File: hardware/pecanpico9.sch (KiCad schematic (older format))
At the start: 119 parts, among them IC1 SPV1040T, IC2 TPS62260DRVR, IC3 ADP322ACPZ-115-R7, IC4 Si4063-B1B-FM, IC5 STM32F413xG, IC6 EVA-7M, IC7 PAC1720-1-AIA-TR, IC8 LDLN015PU33R, IC9 BME280, P1 CONN_01X25, P2 CONN_01X10, P3 ZX62-B-5PA(33), P4 IPX 2mm, P5 CONN_01X02, P6 IPX 2mm, Q1 FDN306P, X1 KT2016K26000BCW18ZAS

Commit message: Wiggled parts around
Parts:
- removed W12, W13, W14, W15, W16, W17, W19, W21, W22, W23, W26, W27: Testpad, stm32f7:Testpad, symbol TEST_1P
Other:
- note added: "Camera connector and Atmosphere sensor"
- note removed: "Camera edge connector and daugther board (camera + additional BME280)"
- note removed: "Clock CTRL may be used to modulate\nthe Si4063. It may also influence the\nclock of the STM32 but only slightly."
- moved on the sheet: C30, C31, C32, C33, C34, C35, C37, C38, C39, C40, C43, C44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

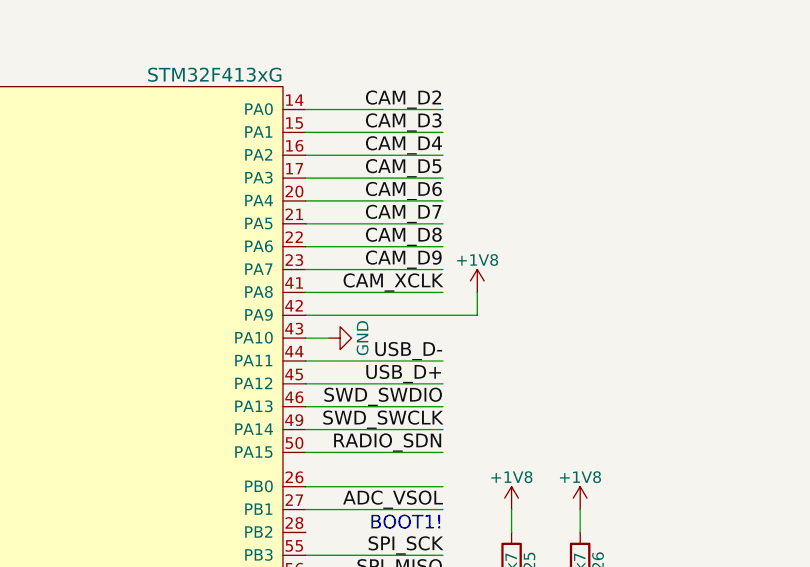
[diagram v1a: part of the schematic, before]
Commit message: Connected VUSB correctly to PA9
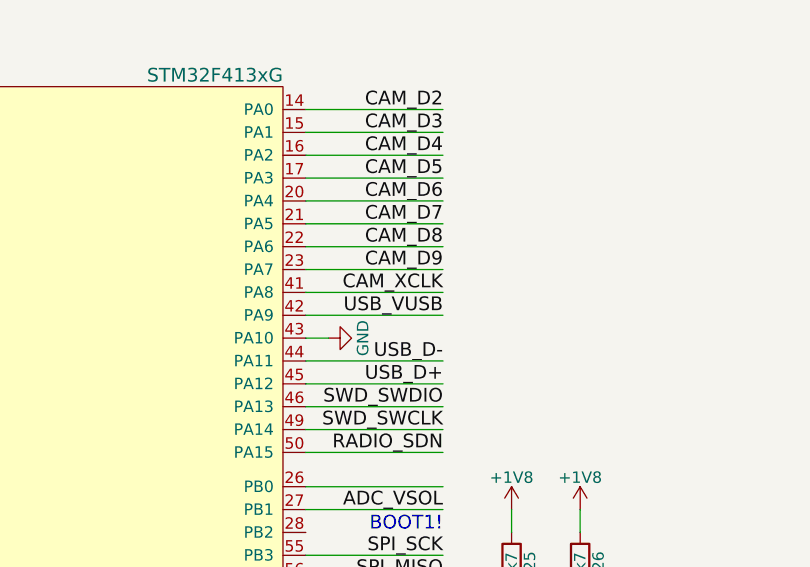
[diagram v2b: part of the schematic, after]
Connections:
- net +1V8: no longer IC5.42 (PA9)
- net USB_VUSB: now also IC5.42 (PA9)
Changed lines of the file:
@@
 BOOT1!
-$Comp
-L +1V8 #PWR097
-U 1 1 58F7653D
-P 19350 4050
-F 0 "#PWR097" H 19350 3900 50  0001 C CNN
-F 1 "+1V8" H 19350 4190 50  0000 C CNN
-F 2 "" H 19350 4050 50  0000 C CNN
-F 3 "" H 19350 4050 50  0000 C CNN
-	1    19350 4050
-	1    0    0    -1
-$EndComp
 $Comp
 L C C35
@@
 $EndComp
 $Comp
-L GND #PWR098
+L GND #PWR097
 U 1 1 58F46541
 P 15000 3650
-F 0 "#PWR098" H 15000 3400 50  0001 C CNN
+F 0 "#PWR097" H 15000 3400 50  0001 C CNN
 F 1 "GND" H 15000 3500 50  0000 C CNN
 F 2 "" H 15000 3650 50  0000 C CNN
@@
 $EndComp
 $Comp
-L GND #PWR099
+L GND #PWR098
 U 1 1 591E7DCF
 P 13300 15000
-F 0 "#PWR099" H 13300 14750 50  0001 C CNN
+F 0 "#PWR098" H 13300 14750 50  0001 C CNN
 F 1 "GND" H 13300 14850 50  0000 C CNN
 F 2 "" H 13300 15000 50  0000 C CNN
@@
 $EndComp
 $Comp
-L GND #PWR0100
+L GND #PWR099
 U 1 1 591ED6A9
 P 13300 13400
-F 0 "#PWR0100" H 13300 13150 50  0001 C CNN
+F 0 "#PWR099" H 13300 13150 50  0001 C CNN
 F 1 "GND" H 13300 13250 50  0000 C CNN
 F 2 "" H 13300 13400 50  0000 C CNN
@@
 $EndComp
 $Comp
-L GND #PWR0101
+L GND #PWR0100
 U 1 1 591F0530
 P 13300 14100
-F 0 "#PWR0101" H 13300 13850 50  0001 C CNN
+F 0 "#PWR0100" H 13300 13850 50  0001 C CNN
 F 1 "GND" H 13300 13950 50  0000 C CNN
 F 2 "" H 13300 14100 50  0000 C CNN
@@
 	2400 4600 2500 4600
 Wire Wire Line
-	18600 4150 19350 4150
-Wire Wire Line
-	19350 4150 19350 4050
+	18600 4150 19200 4150
 Wire Wire Line
 	15000 3250 15000 3350
@@
 Wire Wire Line
 	8650 6700 8100 6700
+Text Label 19200 4150 2    60   ~ 0
+USB_VUSB
 $EndSCHEMATC

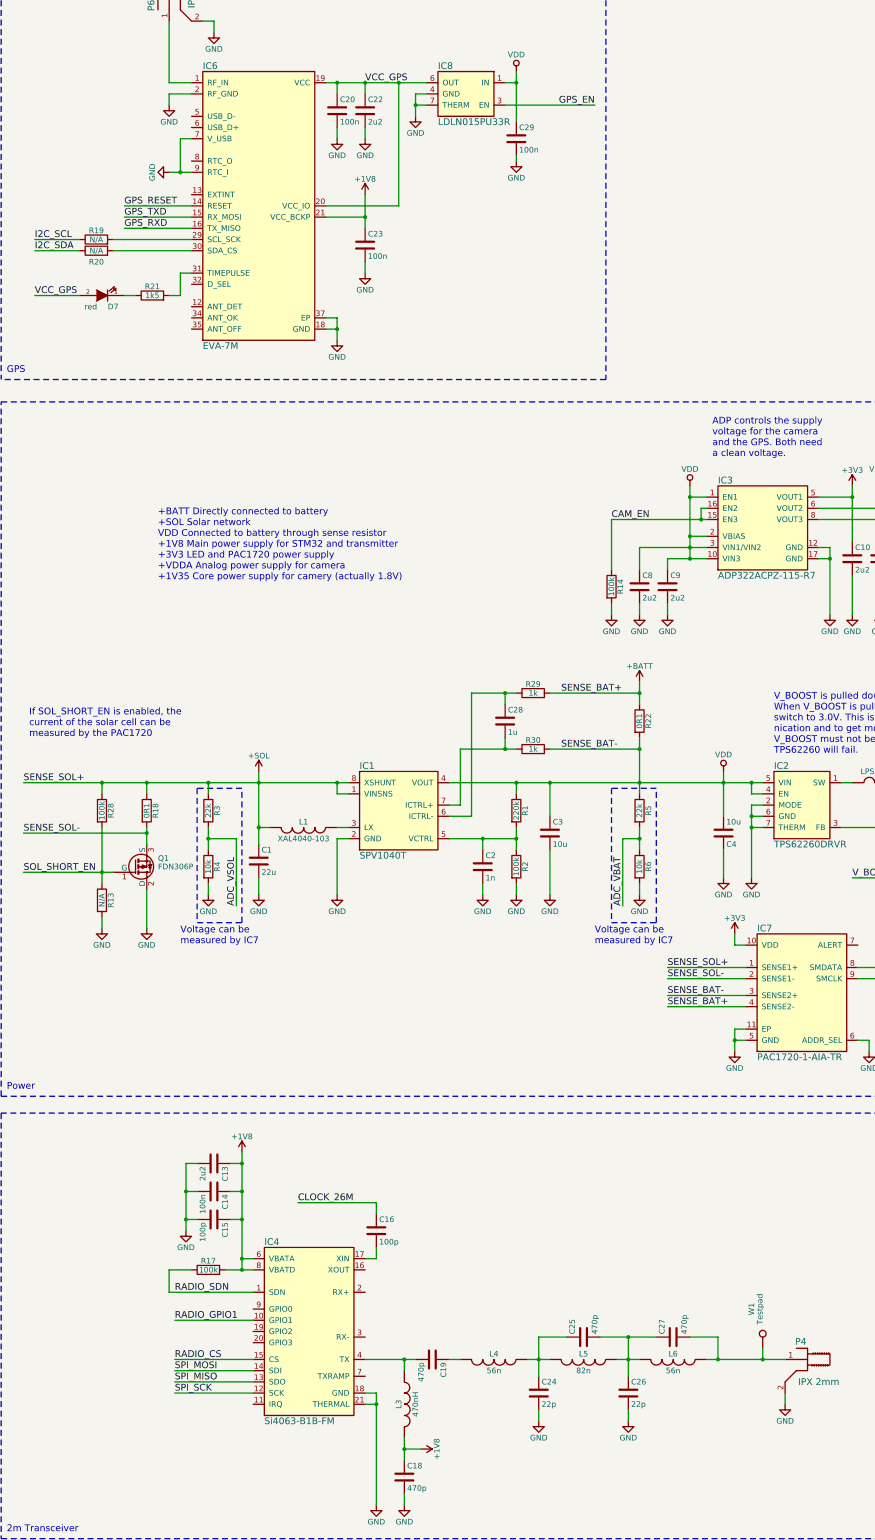
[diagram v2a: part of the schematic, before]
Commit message: Wiggled traces around, created Gerber
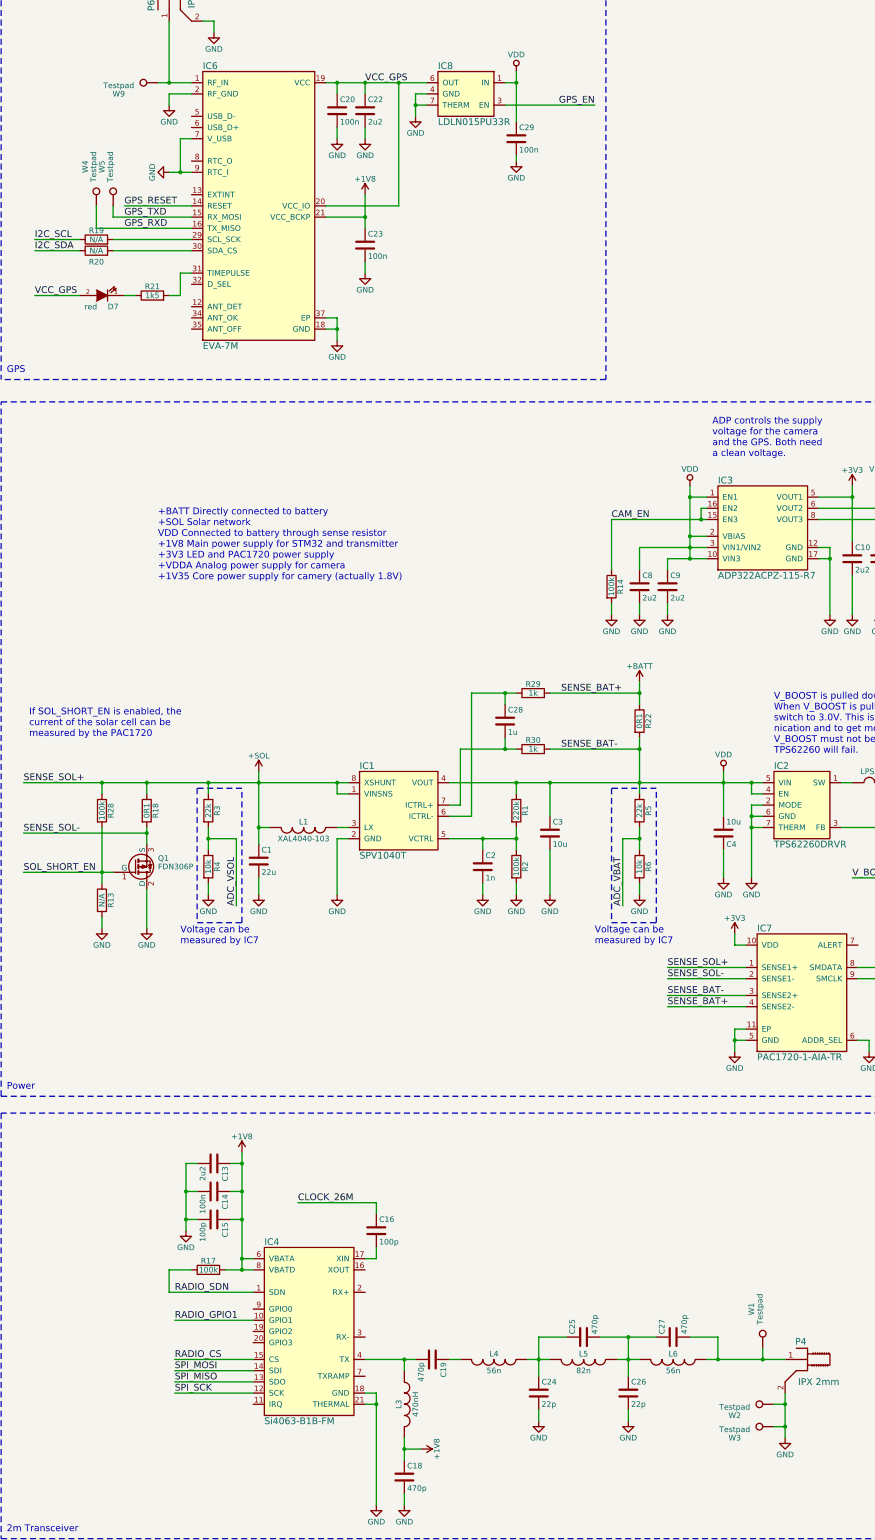
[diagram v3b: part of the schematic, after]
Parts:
- added W2, W3, W9: Testpad, stm32f7:PAD_3x1.5, symbol TEST_1P
- added W4, W5: Testpad, stm32f7:Testpad, symbol TEST_1P
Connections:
- net GND: now also W2.1, W3.1
- net GPS_RXD: now also W4.1
- net GPS_TXD: now also W5.1
- net at IC6.1 (RF_IN), P6.1: now also W9.1

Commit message: Updated BOM
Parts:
- C1, C24, C26, C3, C4, C8, C9: Specs 16V -> 10V
- C32: value 10nF -> 10n
- C5: value 22pF -> 22p
- L3: value 470nH -> 470n
- R18, R22: Mouser 71-WSLP0603R1000FEA -> 667-ERJ-3RSFR10V
- R36, R8: value 250k -> 249k
- R7: value 500k -> 510k
